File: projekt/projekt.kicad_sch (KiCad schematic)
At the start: 28 parts, among them J1 Conn_01x05, J2 USB_B_Micro, J3 Conn_01x03, J4 87583-0010RHLF, U1 MAX17048G_T10, U2 TPS61022RWUT, U3 MCP73871-2CCI_ML

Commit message: MAIN: Work in progress.
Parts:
- removed C10: 10u, symbol Device:C
- removed J2: USB_B_Micro, symbol Connector:USB_B_Micro
- removed J3: Conn_01x03, symbol Connector_Generic:Conn_01x03
- added C5: 10u, symbol Device:C
- added J2: Conn_01x04, symbol Connector_Generic:Conn_01x04
- added J5: 10118192-0001LF, 10118192-0001LF:AMPHENOL_10118192-0001LF, symbol 10118192-0001LF:10118192-0001LF
- L1: footprint (none) -> Inductor_SMD:L_Wuerth_WE-TPC-3816
- R1, R10, R2, R3, R4, R5, R6, R7, R9, RT1, RT2: footprint (none) -> Resistor_SMD:R_0603_1608Metric
- TH1: value NTC 10kOhm 3380K -> NCP18XH103E0SRB; footprint (none) -> Resistor_SMD:R_0603_1608Metric
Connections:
- net +5V_CHARGE: now also C5.1, J5.1 (VUSB)
- net GND: now also C5.2, J2.4 (Pin_4), J5.5 (GND), J5.SH1 (SHIELD), J5.SH2 (SHIELD), J5.SH3 (SHIELD), J5.SH4 (SHIELD), J5.SH5 (SHIELD), J5.SH6 (SHIELD)
- net LBO: now also J2.2 (Pin_2)
- net PG: now also J2.1 (Pin_1)
- net STAT2: now also J2.3 (Pin_3)
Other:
- moved on the sheet: C3, C4, J4, L1, R4, R7, U2

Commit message: MAIN: PCB work in progress.
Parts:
- removed BT1: Battery_Cell, symbol Device:Battery_Cell
- added BT1: 1042P, 1042P:BAT_1042P, symbol 1042P:1042P
- C1, C2: value 100n -> 0.1u; footprint (none) -> Capacitor_SMD:C_0603_1608Metric
- C3, C4, C5, C8, C9: footprint (none) -> Capacitor_SMD:C_0603_1608Metric
- J2: footprint (none) -> Connector_PinHeader_2.54mm:PinHeader_1x04_P2.54mm_Vertical
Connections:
- net +BATT: now also BT1.P
- net GND: now also J1.1 (Pin_1), J2.1 (Pin_1), BT1.N; no longer J1.2 (Pin_2), J2.4 (Pin_4)
- net INT: now also J1.3 (Pin_3); no longer J1.5 (Pin_5)
- net PG: now also J2.4 (Pin_4); no longer J2.1 (Pin_1)
- net SCL: now also J1.4 (Pin_4); no longer J1.3 (Pin_3)
- net SDA: now also J1.5 (Pin_5); no longer J1.4 (Pin_4)
- net V_IN_FG: now also J1.2 (Pin_2); no longer J1.1 (Pin_1)
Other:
- note added: "NOTATKI - Designing a Reverse Polarity Protection Circuit"
- note removed: "NOTATKI - POPRAW ZAKRESE VIN PRZETWORNICY DO 2.8V-5.0V, Popraw I nominal na 1.8A i Imax na 2.5A - Dodaj USB out 5V - Popraw symbole zasilania"

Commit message: MAIN: wersja pierwsza 19.04.
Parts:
- added R11, R12, R13, R8: R, Resistor_SMD:R_0603_1608Metric, symbol Device:R
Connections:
- net +5V_OUT: now also R12.1, R8.1
- net GND: now also R11.2, R13.2
- net D-: now reaches J4.02 (D-)
- net D-: now also R12.2, R13.1
- net D+: now reaches J4.03 (D+)
- net D+: now also R11.1, R8.2
- no-connect marks 5 -> 3
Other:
- note added: "NOTATKI - Designing a Reverse Polarity Protection Circuit - https://learn.adafruit.com/minty-boost/icharging"
- note added: "VOLTAGE DIV (opcjonalne dla urządzeń Apple)"
- note removed: "NOTATKI - Designing a Reverse Polarity Protection Circuit"

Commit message: MAIN: readme.md update
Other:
- company: (none) -> Szymon Gogulski
- title: (none) -> Zasilacz dla urządzeń mobilnych
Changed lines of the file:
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@@
 (kicad_sch (version 20230121) (generator eeschema)
   (paper "A4")
+  (title_block
+    (title "Zasilacz dla urządzeń mobilnych")
+    (date "19.04.2025")
+    (company "Szymon Gogulski")
+  )
   (junction (at 78.74 120.65) (diameter 0) (color 0 0 0 0)
   )

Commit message: MAIN: 23.04 start wersja 2 - poprawki w schemacie.
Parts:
- added C6, C7: 22u, Capacitor_SMD:C_0603_1608Metric, symbol Device:C
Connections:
- net +5V_OUT: now also C6.1, C7.1
- net +BATT: now also C2.1, U1.3 (VDD)
- net GND: now also C6.2, C7.2
- net V_IN_FG: no longer C2.1, J1.2 (Pin_2), R1.1, R2.1, R3.1, U1.3 (VDD)
- new net V_MCU_LOGIC: J1.2 (Pin_2), R1.1, R2.1, R3.1
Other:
- note added: "MAX17048 DOKUMENTACJA The MAX17048 operates with a single lithium cell. The ICs automatically detect when the battery enters a low-current state and enters low-power 3μA hibernate mode, while still providing accurate fuel gauging. The ICs automatically exit hibernate mode when the system returns to active state. VDD = 2.5V to 4.5V CTG - GND CELL - CONNECT TO +BATT VDD - CONNECT TO +BATT GND - GND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"
- note added: "TPS61022 DOKUMENTACJA GND - GND SW - CEWKA do V_LOAD VOUT - +5V_OUT FB - DZIELNIK R1 - 732k; R2 - 100k EN - V_LOAD (ENABLE the device) MODE - GND (Pulse Frequency Modulation, lepsza wydajność zasilacza) VIN - V_LOAD + kondesator 10u - DODAJ PRZEŁĄCZNIK PRZY ENABLE DLA MOŻLIWOŚCI WŁĄCZANIA I WYŁĄCZANIA URZĄDZENIA - DODAJ DIODE PRZY WYJŚCIU +5V_OUT"
- moved on the sheet: BT1, C1, C2, C3, C4, C5, C8, C9, J1, J2, J4, J5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

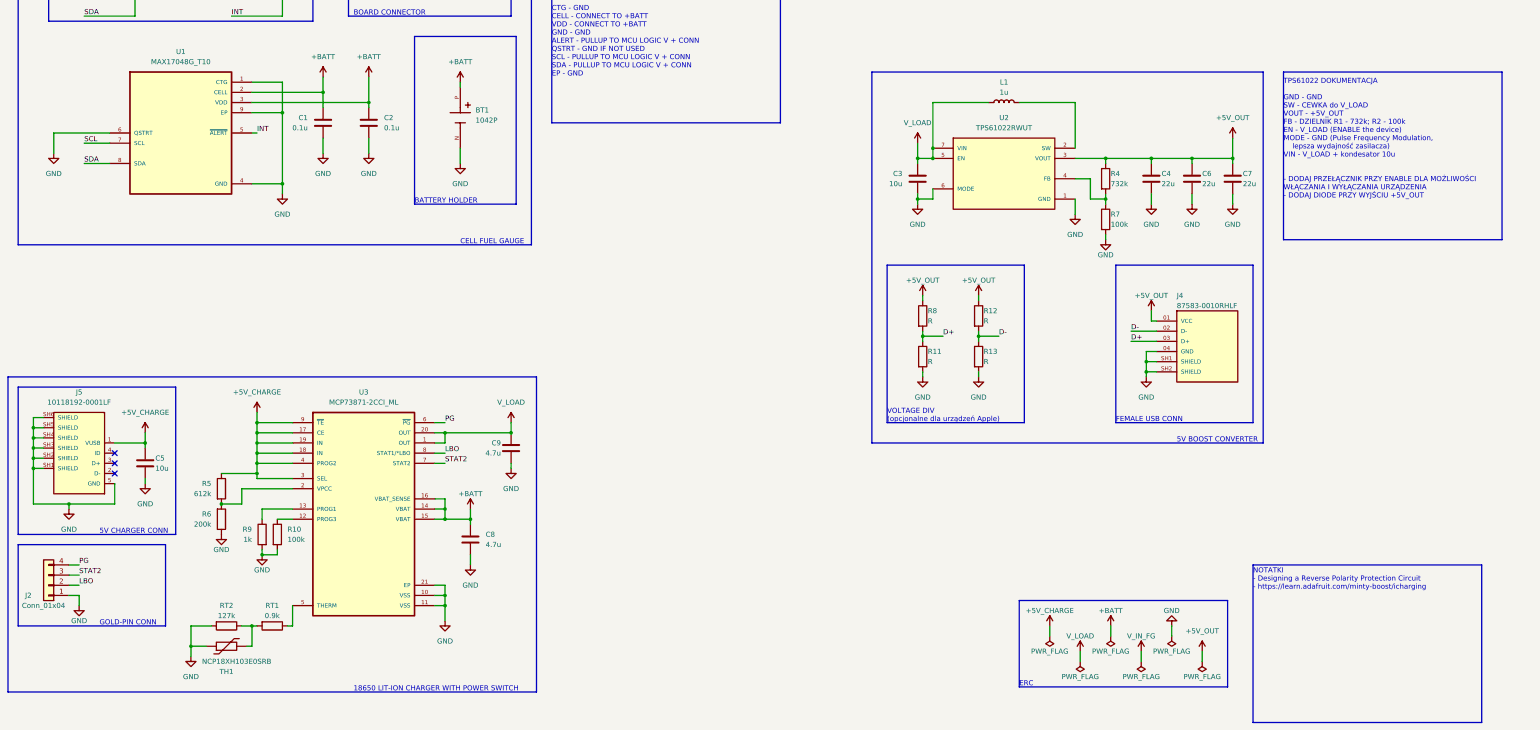
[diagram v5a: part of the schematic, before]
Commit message: MAIN: Wersja 2: poprawki sieci +5V_CHARGE.
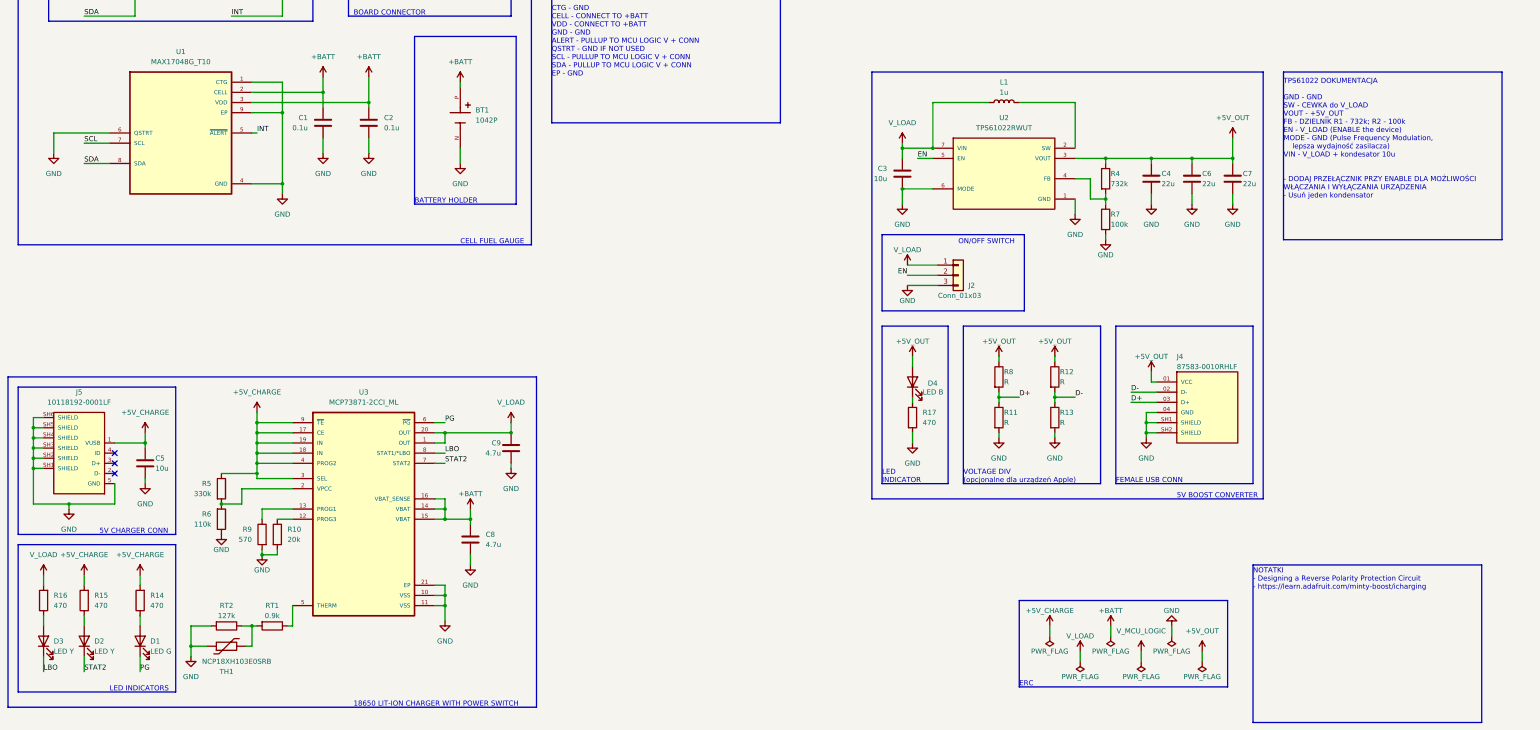
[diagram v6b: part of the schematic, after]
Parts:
- removed J2: Conn_01x04, Connector_PinHeader_2.54mm:PinHeader_1x04_P2.54mm_Vertical, symbol Connector_Generic:Conn_01x04
- added D1: LED G, Diode_SMD:D_0603_1608Metric, symbol Device:LED
- added D2, D3: LED Y, Diode_SMD:D_0603_1608Metric, symbol Device:LED
- added D4: LED B, Diode_SMD:D_0603_1608Metric, symbol Device:LED
- added J2: Conn_01x03, Connector_PinHeader_2.54mm:PinHeader_1x03_P2.54mm_Vertical, symbol Connector_Generic:Conn_01x03
- added R14, R15, R16, R17: 470, Resistor_SMD:R_0603_1608Metric, symbol Device:R
- R10: value 100k -> 20k
- R5: value 612k -> 330k
- R6: value 200k -> 110k
- R9: value 1k -> 570
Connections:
- net +5V_CHARGE: now also R14.2, R15.2
- net +5V_OUT: now also D4.2 (A)
- net GND: now also J2.3 (Pin_3), R17.2
- net LBO: now also D3.1 (K)
- net PG: now also D1.1 (K)
- net STAT2: now also D2.1 (K)
- net V_LOAD: now also J2.1 (Pin_1), R16.2; no longer U2.5 (EN)
- new net: D2.2 (A), R15.1
- new net: D1.2 (A), R14.1
- new net: D3.2 (A), R16.1
- new net: D4.1 (K), R17.1
- new net EN: J2.2 (Pin_2), U2.5 (EN)
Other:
- note added: "LED INDICATOR"
- note added: "LED INDICATORS"
- note added: "ON/OFF SWITCH"
- note added: "TPS61022 DOKUMENTACJA GND - GND SW - CEWKA do V_LOAD VOUT - +5V_OUT FB - DZIELNIK R1 - 732k; R2 - 100k EN - V_LOAD (ENABLE the device) MODE - GND (Pulse Frequency Modulation, lepsza wydajność zasilacza) VIN - V_LOAD + kondesator 10u - DODAJ PRZEŁĄCZNIK PRZY ENABLE DLA MOŻLIWOŚCI WŁĄCZANIA I WYŁĄCZANIA URZĄDZENIA - Usuń jeden kondensator"
- note removed: "GOLD-PIN CONN"
- note removed: "TPS61022 DOKUMENTACJA GND - GND SW - CEWKA do V_LOAD VOUT - +5V_OUT FB - DZIELNIK R1 - 732k; R2 - 100k EN - V_LOAD (ENABLE the device) MODE - GND (Pulse Frequency Modulation, lepsza wydajność zasilacza) VIN - V_LOAD + kondesator 10u - DODAJ PRZEŁĄCZNIK PRZY ENABLE DLA MOŻLIWOŚCI WŁĄCZANIA I WYŁĄCZANIA URZĄDZENIA - DODAJ DIODE PRZY WYJŚCIU +5V_OUT"
- moved on the sheet: C3, J4, R11, R12, R13, R8

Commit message: MAIN: Wersja 2. Sprawdzenie reguł produkcyjnych. Test wykonania u producenta.
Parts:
- added H1, H2, H3: MountingHole, MountingHole:MountingHole_2.2mm_M2, symbol Mechanical:MountingHole
- added TP1, TP2, TP3, TP4: TestPoint, TestPoint:TestPoint_THTPad_1.0x1.0mm_Drill0.5mm, symbol Connector:TestPoint
- added TP5, TP6, TP7, TP8: TestPoint, TestPoint:TestPoint_THTPad_D1.0mm_Drill0.5mm, symbol Connector:TestPoint
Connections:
- net +5V_CHARGE: now also TP6.1
- net +5V_OUT: now also TP8.1
- net +BATT: now also TP5.1
- net GND: now also TP1.1, TP2.1, TP3.1, TP4.1
- net V_LOAD: now also TP7.1
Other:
- note added: "Montaż"
- note added: "TPS61022 DOKUMENTACJA GND - GND SW - CEWKA do V_LOAD VOUT - +5V_OUT FB - DZIELNIK R1 - 732k; R2 - 100k EN - V_LOAD (ENABLE the device) MODE - GND (Pulse Frequency Modulation, lepsza wydajność zasilacza) VIN - V_LOAD + kondesator 10u"
- note removed: "TPS61022 DOKUMENTACJA GND - GND SW - CEWKA do V_LOAD VOUT - +5V_OUT FB - DZIELNIK R1 - 732k; R2 - 100k EN - V_LOAD (ENABLE the device) MODE - GND (Pulse Frequency Modulation, lepsza wydajność zasilacza) VIN - V_LOAD + kondesator 10u - DODAJ PRZEŁĄCZNIK PRZY ENABLE DLA MOŻLIWOŚCI WŁĄCZANIA I WYŁĄCZANIA URZĄDZENIA - Usuń jeden kondensator"
- moved on the sheet: BT1, C1, C2, C5, C8, C9, D1, D2, D3, J1, J5, R1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

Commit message: MAIN: wersja 2, dodałem modele 3D.
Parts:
- L1: footprint Inductor_SMD:L_Wuerth_WE-TPC-3816 -> WE-TCP_3816:WE-TPC_3816
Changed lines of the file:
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@@
       (effects (font (size 1.27 1.27)))
     )
-    (property "Footprint" "Inductor_SMD:L_Wuerth_WE-TPC-3816" (at 279.4 93.98 0)
+    (property "Footprint" "WE-TCP_3816:WE-TPC_3816" (at 279.4 93.98 0)
       (effects (font (size 1.27 1.27)) hide)
     )
